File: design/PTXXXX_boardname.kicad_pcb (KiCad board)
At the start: 4 copper layers, 150 x 100 mm, 4 parts

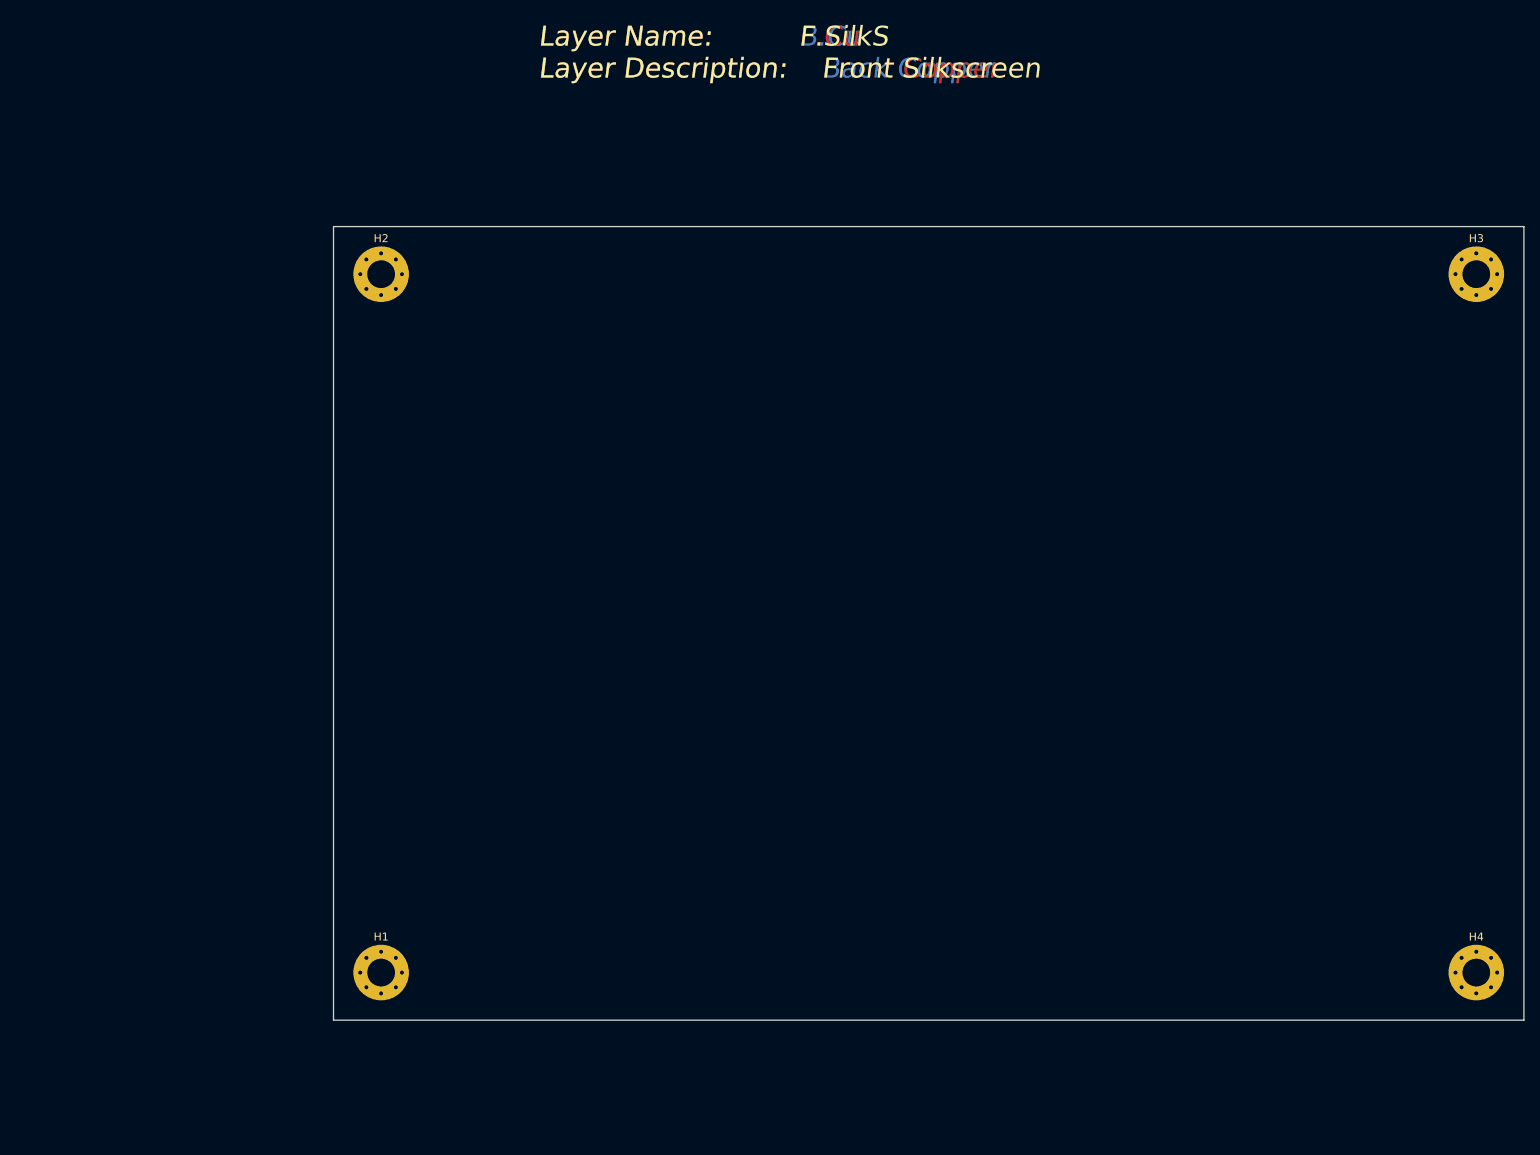
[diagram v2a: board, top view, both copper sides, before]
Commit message: added silkscreen logo & PCB ID (locally in PCB design, not using footprints) added GND copper planes on all 4 layers (0.4mm clearance/0.25mm for same-net) updated library refs updated template design with library symb/fp library tables from kicad-library submodule
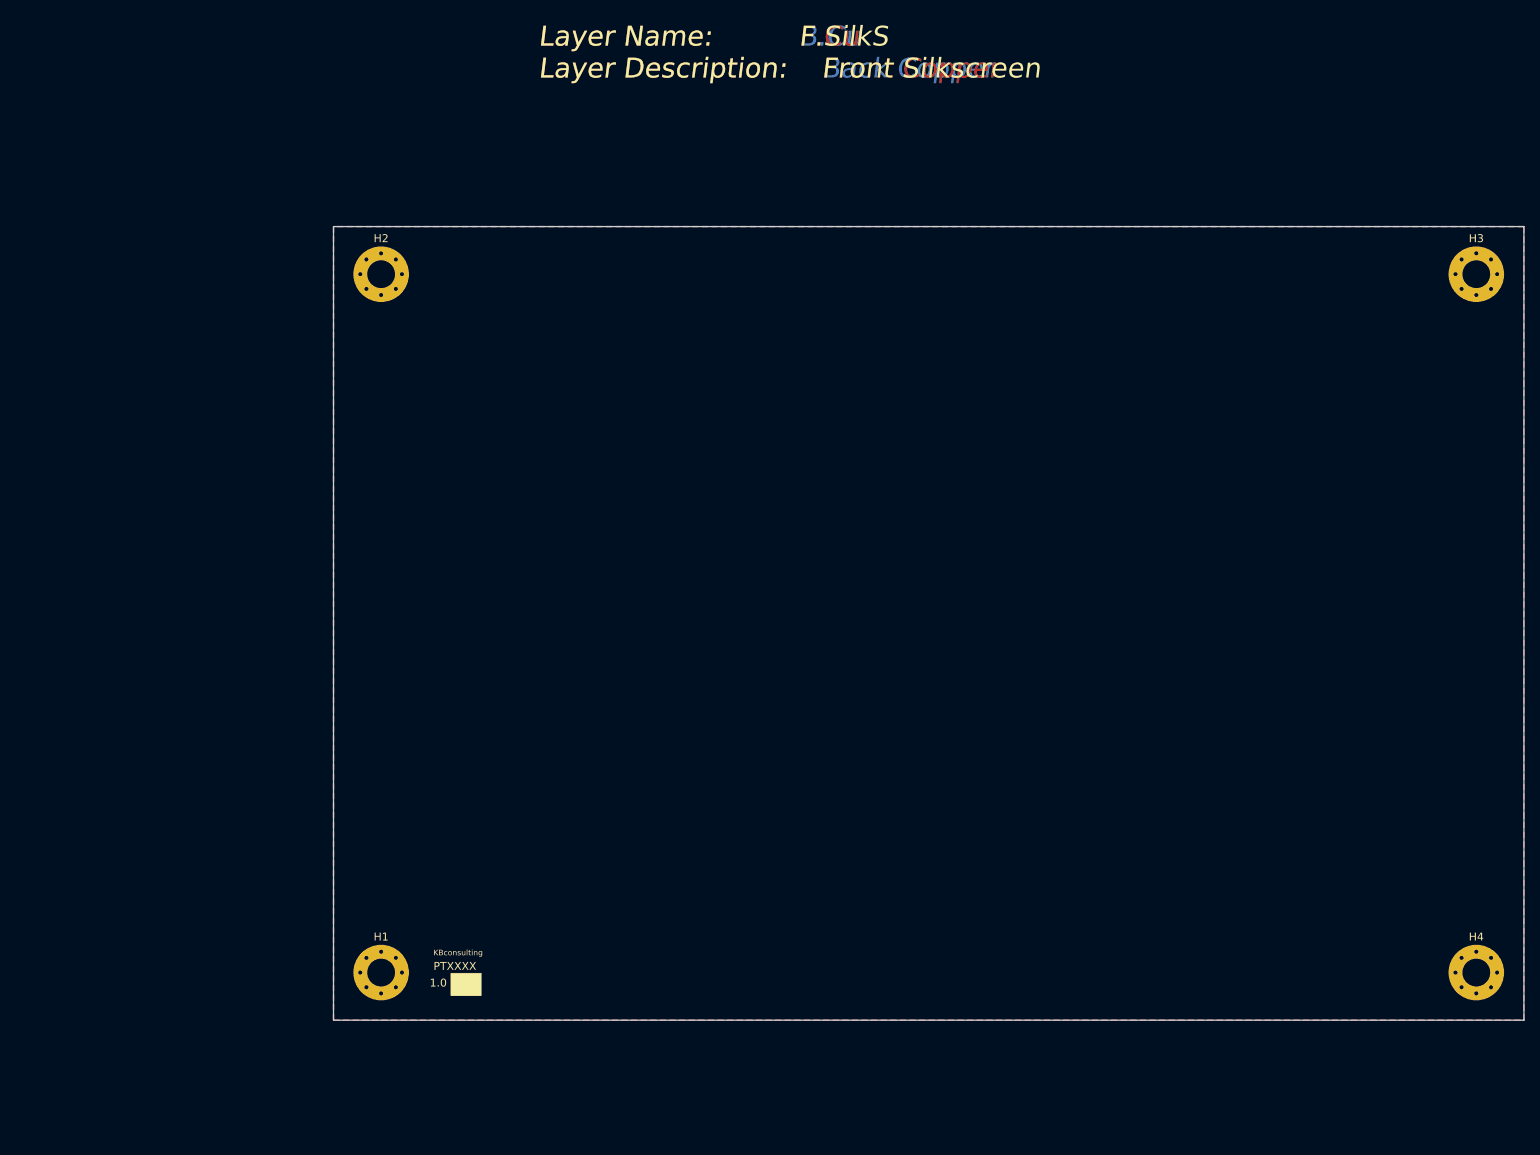
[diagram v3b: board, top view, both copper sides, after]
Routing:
- added copper zone on B.Cu, net GND
- added copper zone on F.Cu, net GND
- added copper zone on In1.Cu, net GND
- added copper zone on In2.Cu, net GND
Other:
- board text added: "1.0"
- board text added: "KBconsulting"
- board text added: "PTXXXX"
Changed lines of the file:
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@@
   (general
     (thickness 1.6)
-    (drawings 29)
+    (drawings 32)
     (tracks 0)
     (zones 0)
@@
     (user_trace_width 3)
     (trace_clearance 0.25)
-    (zone_clearance 0.508)
+    (zone_clearance 0.4)
     (zone_45_only no)
     (trace_min 0.25)
@@
   )
   (module MountingHole:MountingHole_3.5mm_Pad_Via (layer F.Cu)
-    (at 86 139)
+    (at 224 139)
     (descr "Mounting Hole 3.5mm")
     (tags "mounting hole 3.5mm")
     (attr virtual)
-    (fp_text reference H1 (at 0 -4.5) (layer F.SilkS)
+    (fp_text reference H4 (at 0 -4.5) (layer F.SilkS)
       (effects (font (size 1 1) (thickness 0.15)))
     )
@@
       (effects (font (size 1 1) (thickness 0.15)))
     )
+    (fp_circle (center 0 0) (end 3.75 0) (layer F.CrtYd) (width 0.05))
+    (fp_circle (center 0 0) (end 3.5 0) (layer Cmts.User) (width 0.15))
     (fp_text user %R (at 0.3 0) (layer F.Fab)
       (effects (font (size 1 1) (thickness 0.15)))
     )
+    (pad 1 thru_hole circle (at 1.856155 -1.856155) (size 0.8 0.8) (drill 0.5) (layers *.Cu *.Mask)
+      (net 1 GND))
+    (pad 1 thru_hole circle (at 0 -2.625) (size 0.8 0.8) (drill 0.5) (layers *.Cu *.Mask)
+      (net 1 GND))
+    (pad 1 thru_hole circle (at -1.856155 -1.856155) (size 0.8 0.8) (drill 0.5) (layers *.Cu *.Mask)
+      (net 1 GND))
+    (pad 1 thru_hole circle (at -2.625 0) (size 0.8 0.8) (drill 0.5) (layers *.Cu *.Mask)
+      (net 1 GND))
+    (pad 1 thru_hole circle (at -1.856155 1.856155) (size 0.8 0.8) (drill 0.5) (layers *.Cu *.Mask)
+      (net 1 GND))
+    (pad 1 thru_hole circle (at 0 2.625) (size 0.8 0.8) (drill 0.5) (layers *.Cu *.Mask)
+      (net 1 GND))
+    (pad 1 thru_hole circle (at 1.856155 1.856155) (size 0.8 0.8) (drill 0.5) (layers *.Cu *.Mask)
+      (net 1 GND))
+    (pad 1 thru_hole circle (at 2.625 0) (size 0.8 0.8) (drill 0.5) (layers *.Cu *.Mask)
+      (net 1 GND))
+    (pad 1 thru_hole circle (at 0 0) (size 7 7) (drill 3.5) (layers *.Cu *.Mask)
+      (net 1 GND))
+  )
+  (module MountingHole:MountingHole_3.5mm_Pad_Via (layer F.Cu)
+    (at 224 51)
+    (descr "Mounting Hole 3.5mm")
+    (tags "mounting hole 3.5mm")
+    (attr virtual)
+    (fp_text reference H3 (at 0 -4.5) (layer F.SilkS)
+      (effects (font (size 1 1) (thickness 0.15)))
+    )
+    (fp_text value "M3 Hole" (at 0 4.5) (layer F.Fab)
+      (effects (font (size 1 1) (thickness 0.15)))
+    )
+    (fp_circle (center 0 0) (end 3.75 0) (layer F.CrtYd) (width 0.05))
     (fp_circle (center 0 0) (end 3.5 0) (layer Cmts.User) (width 0.15))
-    (fp_circle (center 0 0) (end 3.75 0) (layer F.CrtYd) (width 0.05))
+    (fp_text user %R (at 0.3 0) (layer F.Fab)
+      (effects (font (size 1 1) (thickness 0.15)))
+    )
+    (pad 1 thru_hole circle (at 1.856155 -1.856155) (size 0.8 0.8) (drill 0.5) (layers *.Cu *.Mask)
+      (net 1 GND))
+    (pad 1 thru_hole circle (at 0 -2.625) (size 0.8 0.8) (drill 0.5) (layers *.Cu *.Mask)
+      (net 1 GND))
+    (pad 1 thru_hole circle (at -1.856155 -1.856155) (size 0.8 0.8) (drill 0.5) (layers *.Cu *.Mask)
+      (net 1 GND))
+    (pad 1 thru_hole circle (at -2.625 0) (size 0.8 0.8) (drill 0.5) (layers *.Cu *.Mask)
+      (net 1 GND))
+    (pad 1 thru_hole circle (at -1.856155 1.856155) (size 0.8 0.8) (drill 0.5) (layers *.Cu *.Mask)
+      (net 1 GND))
+    (pad 1 thru_hole circle (at 0 2.625) (size 0.8 0.8) (drill 0.5) (layers *.Cu *.Mask)
+      (net 1 GND))
+    (pad 1 thru_hole circle (at 1.856155 1.856155) (size 0.8 0.8) (drill 0.5) (layers *.Cu *.Mask)
+      (net 1 GND))
+    (pad 1 thru_hole circle (at 2.625 0) (size 0.8 0.8) (drill 0.5) (layers *.Cu *.Mask)
+      (net 1 GND))
     (pad 1 thru_hole circle (at 0 0) (size 7 7) (drill 3.5) (layers *.Cu *.Mask)
-      (net 1 GND))
-    (pad 1 thru_hole circle (at 2.625 0) (size 0.8 0.8) (drill 0.5) (layers *.Cu *.Mask)
-      (net 1 GND))
-    (pad 1 thru_hole circle (at 1.856155 1.856155) (size 0.8 0.8) (drill 0.5) (layers *.Cu *.Mask)
-      (net 1 GND))
-    (pad 1 thru_hole circle (at 0 2.625) (size 0.8 0.8) (drill 0.5) (layers *.Cu *.Mask)
-      (net 1 GND))
-    (pad 1 thru_hole circle (at -1.856155 1.856155) (size 0.8 0.8) (drill 0.5) (layers *.Cu *.Mask)
-      (net 1 GND))
-    (pad 1 thru_hole circle (at -2.625 0) (size 0.8 0.8) (drill 0.5) (layers *.Cu *.Mask)
-      (net 1 GND))
-    (pad 1 thru_hole circle (at -1.856155 -1.856155) (size 0.8 0.8) (drill 0.5) (layers *.Cu *.Mask)
-      (net 1 GND))
-    (pad 1 thru_hole circle (at 0 -2.625) (size 0.8 0.8) (drill 0.5) (layers *.Cu *.Mask)
-      (net 1 GND))
-    (pad 1 thru_hole circle (at 1.856155 -1.856155) (size 0.8 0.8) (drill 0.5) (layers *.Cu *.Mask)
       (net 1 GND))
   )
@@
   )
   (module MountingHole:MountingHole_3.5mm_Pad_Via (layer F.Cu)
-    (at 224 51)
+    (at 86 139)
     (descr "Mounting Hole 3.5mm")
     (tags "mounting hole 3.5mm")
     (attr virtual)
-    (fp_text reference H3 (at 0 -4.5) (layer F.SilkS)
-      (effects (font (size 1 1) (thickness 0.15)))
-    )
-    (fp_text value "M3 Hole" (at 0 4.5) (layer F.Fab)
-      (effects (font (size 1 1) (thickness 0.15)))
-    )
-    (fp_text user %R (at 0.3 0) (layer F.Fab)
-      (effects (font (size 1 1) (thickness 0.15)))
-    )
-    (fp_circle (center 0 0) (end 3.5 0) (layer Cmts.User) (width 0.15))
-    (fp_circle (center 0 0) (end 3.75 0) (layer F.CrtYd) (width 0.05))
-    (pad 1 thru_hole circle (at 0 0) (size 7 7) (drill 3.5) (layers *.Cu *.Mask)
-      (net 1 GND))
-    (pad 1 thru_hole circle (at 2.625 0) (size 0.8 0.8) (drill 0.5) (layers *.Cu *.Mask)
-      (net 1 GND))
-    (pad 1 thru_hole circle (at 1.856155 1.856155) (size 0.8 0.8) (drill 0.5) (layers *.Cu *.Mask)
-      (net 1 GND))
-    (pad 1 thru_hole circle (at 0 2.625) (size 0.8 0.8) (drill 0.5) (layers *.Cu *.Mask)
-      (net 1 GND))
-    (pad 1 thru_hole circle (at -1.856155 1.856155) (size 0.8 0.8) (drill 0.5) (layers *.Cu *.Mask)
-      (net 1 GND))
-    (pad 1 thru_hole circle (at -2.625 0) (size 0.8 0.8) (drill 0.5) (layers *.Cu *.Mask)
-      (net 1 GND))
-    (pad 1 thru_hole circle (at -1.856155 -1.856155) (size 0.8 0.8) (drill 0.5) (layers *.Cu *.Mask)
-      (net 1 GND))
-    (pad 1 thru_hole circle (at 0 -2.625) (size 0.8 0.8) (drill 0.5) (layers *.Cu *.Mask)
-      (net 1 GND))
-    (pad 1 thru_hole circle (at 1.856155 -1.856155) (size 0.8 0.8) (drill 0.5) (layers *.Cu *.Mask)
-      (net 1 GND))
-  )
-  (module MountingHole:MountingHole_3.5mm_Pad_Via (layer F.Cu)
-    (at 224 139)
-    (descr "Mounting Hole 3.5mm")
-    (tags "mounting hole 3.5mm")
-    (attr virtual)
-    (fp_text reference H4 (at 0 -4.5) (layer F.SilkS)
+    (fp_text reference H1 (at 0 -4.5) (layer F.SilkS)
       (effects (font (size 1 1) (thickness 0.15)))
     )
@@
       (net 1 GND))
   )
+  (gr_text KBconsulting (at 95.7 136.5) (layer F.SilkS)
+    (effects (font (size 0.7 0.7) (thickness 0.12)))
+  )
+  (gr_text 1.0 (at 93.2 140.3) (layer F.SilkS)
+    (effects (font (size 1 1) (thickness 0.15)))
+  )
+  (gr_text PTXXXX (at 95.3 138.2) (layer F.SilkS)
+    (effects (font (size 1 1) (thickness 0.15)))
+  )
+  (gr_poly (pts (xy 94.8 139.1) (xy 94.8 141.9) (xy 98.6 141.9) (xy 98.6 139.1)) (layer F.SilkS) (width 0.1))
   (gr_text "Layer Name:          In2.Cu\nLayer Description:    Inner Layer-2 Copper" (at 106 23) (layer In2.Cu)
     (effects (font (size 2.5 2.5) (thickness 0.25) italic) (justify left))
@@
     (effects (font (size 2.5 2.5) (thickness 0.25) italic) (justify left))
   )
-  (target plus (at 80 145) (size 5) (width 0.05) (layer Edge.Cuts))
   (target plus (at 80 145) (size 5) (width 0.05) (layer Edge.Cuts))
   (gr_line (start 228.5 143.5) (end 81.5 143.5) (layer Margin) (width 0.15))
@@
   (gr_line (start 230 145) (end 230 45) (layer Edge.Cuts) (width 0.05))
   (gr_line (start 80 145) (end 230 145) (layer Edge.Cuts) (width 0.05))
+  (zone (net 1) (net_name GND) (layer F.Cu) (hatch edge 0.508)
+    (connect_pads (clearance 0.4))
+    (min_thickness 0.25)
+    (fill yes (arc_segments 32) (thermal_gap 0.251) (thermal_bridge_width 0.251))
+    (polygon
+      (pts
+        (xy 80 45) (xy 80 145) (xy 230 145) (xy 230 45)
+      )
+    )
+  )
+  (zone (net 1) (net_name GND) (layer In1.Cu) (hatch edge 0.508)
+    (connect_pads (clearance 0.4))
+    (min_thickness 0.25)
+    (fill yes (arc_segments 32) (thermal_gap 0.251) (thermal_bridge_width 0.251))
+    (polygon
+      (pts
+        (xy 80 45) (xy 80 145) (xy 230 145) (xy 230 45)
+      )
+    )
+  )
+  (zone (net 1) (net_name GND) (layer In2.Cu) (hatch edge 0.508)
+    (connect_pads (clearance 0.4))
+    (min_thickness 0.25)
+    (fill yes (arc_segments 32) (thermal_gap 0.251) (thermal_bridge_width 0.251))
+    (polygon
+      (pts
+        (xy 80 45) (xy 80 145) (xy 230 145) (xy 230 45)
+      )
+    )
+  )
+  (zone (net 1) (net_name GND) (layer B.Cu) (hatch edge 0.508)
+    (connect_pads (clearance 0.4))
+    (min_thickness 0.25)
+    (fill yes (arc_segments 32) (thermal_gap 0.251) (thermal_bridge_width 0.251))
+    (polygon
+      (pts
+        (xy 80 45) (xy 80 145) (xy 230 145) (xy 230 45)
+      )
+    )
+  )
 )

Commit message: added fabrication PCB specification text to F.Fab layer moved board, origins etc to give more space
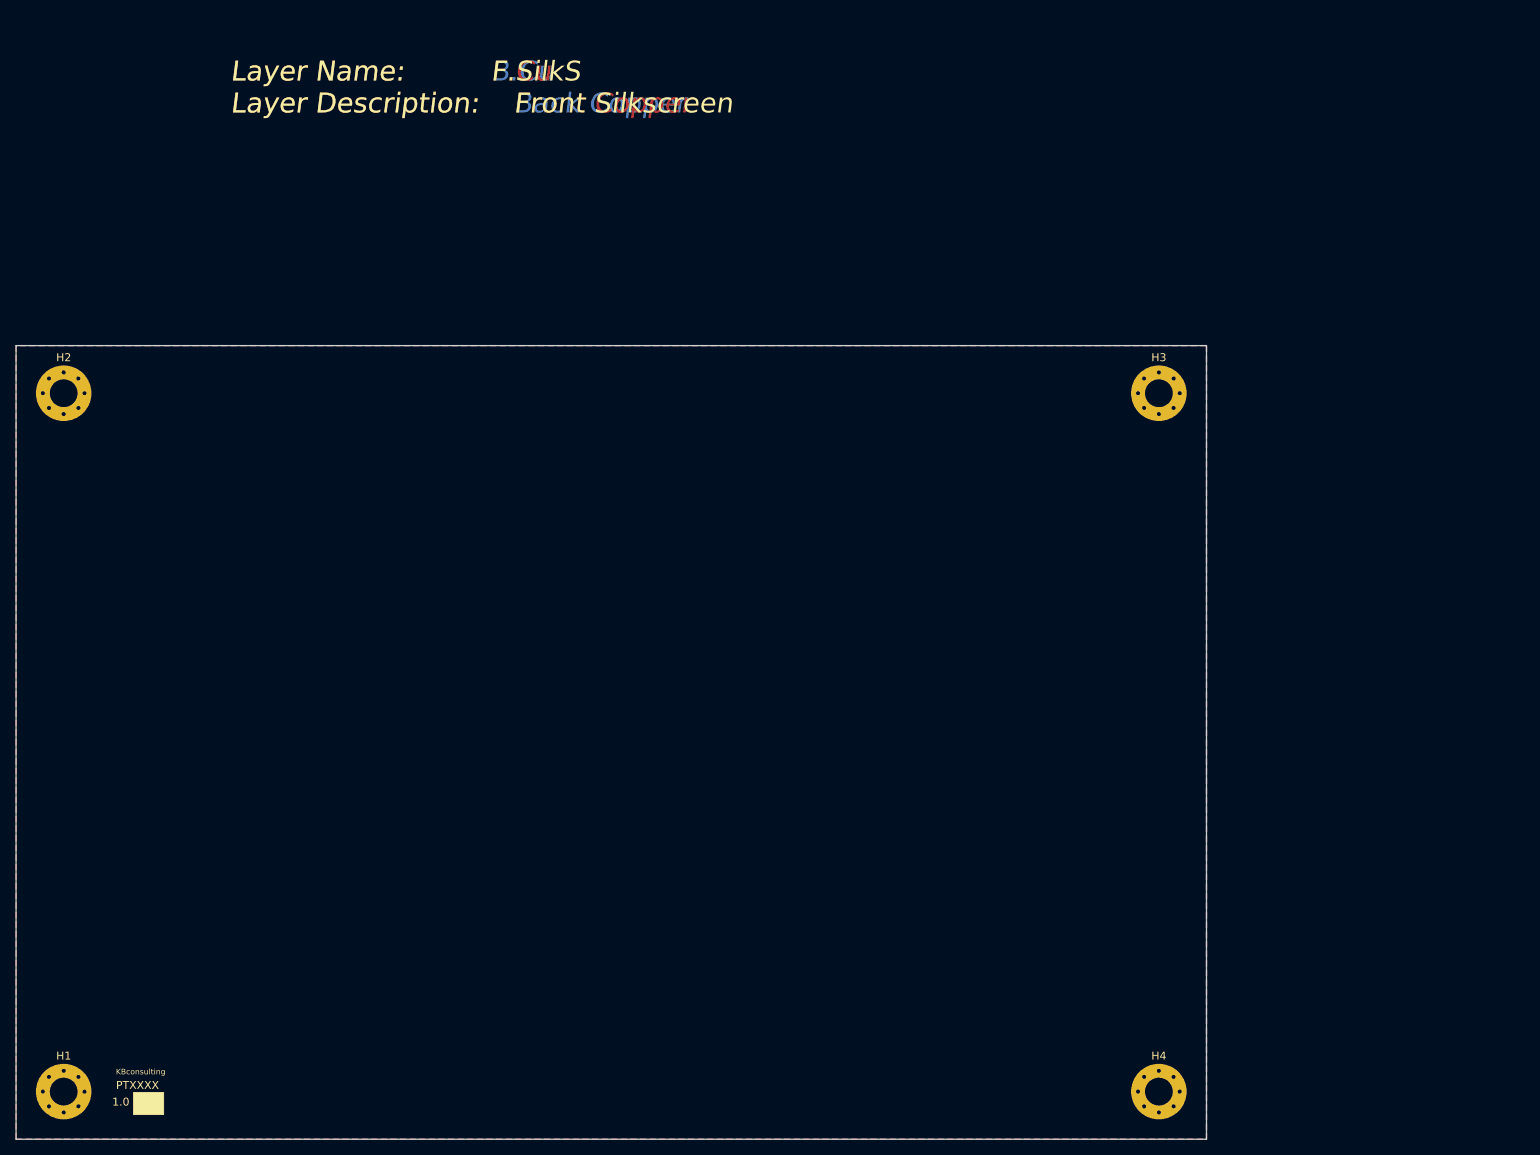
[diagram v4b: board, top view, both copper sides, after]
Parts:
- moved H1 42.7 mm to (46.0, 154.0)
- moved H2 42.7 mm to (46.0, 66.0)
- moved H3 42.7 mm to (184.0, 66.0)
- moved H4 42.7 mm to (184.0, 154.0)
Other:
- board text added: "FABRICATION =========== SUMMARY: LAYER COUNT: DESIGN RULES: IMPEDANCE CONTROL: MATERIAL: COPPER WEIGHT: FINISH: RESIST COLOUR: SILKSCREEN COLOUR: DIMENSIONS: FINISHED THICKNESS: EDGE PLATING: EDGE CONNECTORS: EDGE CHAMFERING: THIEVING/VENTING: ROHS/LEAD FREE: DRILLING: PLUGGING: OTHER NOTES:"
- board text added: "INSTRUCTIONS: =========== MULTILAYER, SURFACE MOUNT & THROUGH HOLE 4 (2 SIGNAL & POUR, 2 SPLIT PLANE) MIN 0.2MM TRACK / 0.20MM GAP / 0.30MM DRILL 90Z DIFF PAIR, OUTER (0.25MM TRACK / 0.15MM GAP / 0.12MM TO INNER) FR4 OR EQUIVALENT, PCB RATED UL94V-0 35um OUTERS AND 17.5um INNERS ENIG GREEN WHITE ??.0MM X ??.0MM 1.6MM +/- 10% MAX OVER PLATING NOT REQUIRED NOT REQUIRED NOT REQUIRED SEEK APPROVAL YE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"
